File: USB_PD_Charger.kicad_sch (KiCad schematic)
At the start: 43 parts, among them J9 Conn_01x05, Q1 AON7403, U1 LM3489QMM/NOPB, U2 TPS65987DDHRSHR, U3 MX25L8006EM1I-12G

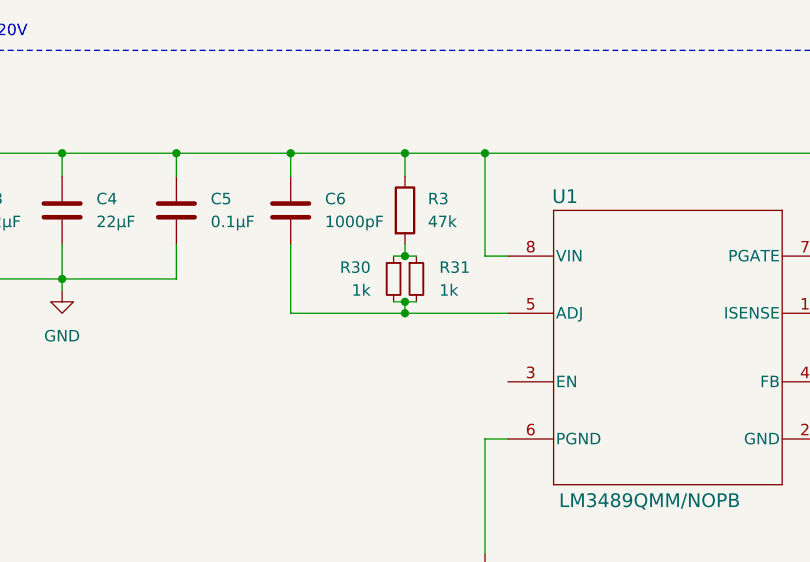
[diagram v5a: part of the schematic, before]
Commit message: Laid out components for power circuits
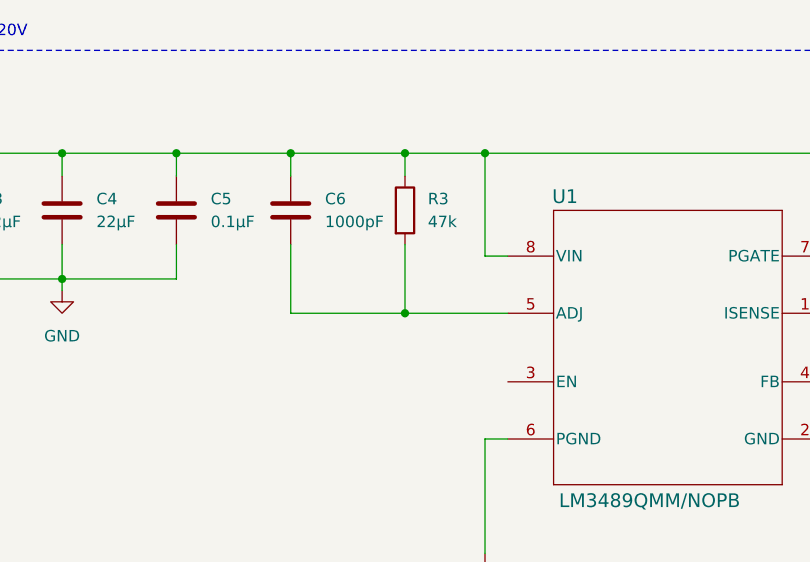
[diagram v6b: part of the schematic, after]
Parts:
- removed R30, R31: 1k, Resistor_SMD:R_0402_1005Metric, symbol Device:R_Small
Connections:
- net at R3.2: now also C6.2, U1.5 (ADJ)
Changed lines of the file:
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@@
 	)
 	(junction
-		(at 99.06 44.45)
-		(diameter 0)
-		(color 0 0 0 0)
-	)
-	(junction
 		(at 166.37 33.02)
 		(diameter 0)
@@
 	)
 	(junction
-		(at 99.06 50.8)
-		(diameter 0)
-		(color 0 0 0 0)
-	)
-	(junction
 		(at 231.14 113.03)
 		(diameter 0)
@@
 	)
 	(junction
-		(at 175.26 33.02)
+		(at 99.06 50.8)
 		(diameter 0)
 		(color 0 0 0 0)
 	)
 	(junction
-		(at 99.06 49.53)
+		(at 175.26 33.02)
 		(diameter 0)
 		(color 0 0 0 0)
@@
 	(wire
 		(pts
-			(xy 99.06 49.53) (xy 100.33 49.53)
-		)
-		(stroke
-			(width 0)
-			(type default)
-		)
-	)
-	(wire
-		(pts
 			(xy 109.22 125.73) (xy 111.76 125.73)
 		)
@@
 	(wire
 		(pts
-			(xy 99.06 43.18) (xy 99.06 44.45)
-		)
-		(stroke
-			(width 0)
-			(type default)
-		)
-	)
-	(wire
-		(pts
 			(xy 196.85 69.85) (xy 194.31 69.85)
 		)
@@
 	(wire
 		(pts
+			(xy 99.06 50.8) (xy 110.49 50.8)
+		)
+		(stroke
+			(width 0)
+			(type default)
+		)
+	)
+	(wire
+		(pts
 			(xy 252.73 31.75) (xy 252.73 33.02)
 		)
@@
 	(wire
 		(pts
-			(xy 86.36 50.8) (xy 99.06 50.8)
-		)
-		(stroke
-			(width 0)
-			(type default)
-		)
-	)
-	(wire
-		(pts
 			(xy 109.22 140.97) (xy 116.84 140.97)
 		)
@@
 	(wire
 		(pts
-			(xy 99.06 50.8) (xy 110.49 50.8)
+			(xy 86.36 50.8) (xy 99.06 50.8)
 		)
 		(stroke
@@
 	(wire
 		(pts
-			(xy 97.79 49.53) (xy 99.06 49.53)
-		)
-		(stroke
-			(width 0)
-			(type default)
-		)
-	)
-	(wire
-		(pts
 			(xy 142.24 121.92) (xy 142.24 120.65)
 		)
@@
 	(wire
 		(pts
-			(xy 99.06 44.45) (xy 100.33 44.45)
-		)
-		(stroke
-			(width 0)
-			(type default)
-		)
-	)
-	(wire
-		(pts
 			(xy 17.78 140.97) (xy 17.78 143.51)
 		)
@@
 	(wire
 		(pts
-			(xy 99.06 44.45) (xy 97.79 44.45)
+			(xy 99.06 43.18) (xy 99.06 50.8)
 		)
 		(stroke
@@
 	(wire
 		(pts
-			(xy 99.06 49.53) (xy 99.06 50.8)
-		)
-		(stroke
-			(width 0)
-			(type default)
-		)
-	)
-	(wire
-		(pts
 			(xy 146.05 44.45) (xy 156.21 44.45)
 		)
@@
 	)
 	(symbol
-		(lib_id "Device:R_Small")
-		(at 100.33 46.99 0)
-		(unit 1)
-		(exclude_from_sim no)
-		(in_bom yes)
-		(on_board yes)
-		(dnp no)
-		(property "Reference" "R31"
-			(at 102.87 45.7199 0)
-			(effects
-				(font
-					(size 1.27 1.27)
-				)
-				(justify left)
-			)
-		)
-		(property "Value" "1k"
-			(at 102.87 48.2599 0)
-			(effects
-				(font
-					(size 1.27 1.27)
-				)
-				(justify left)
-			)
-		)
-		(property "Footprint" "Resistor_SMD:R_0402_1005Metric"
-			(at 100.33 46.99 0)
-			(effects
-				(font
-					(size 1.27 1.27)
-				)
-				(hide yes)
-			)
-		)
-		(property "Datasheet" "~"
-			(at 100.33 46.99 0)
-			(effects
-				(font
-					(size 1.27 1.27)
-				)
-				(hide yes)
-			)
-		)
-		(property "Description" "Resistor, small symbol"
-			(at 100.33 46.99 0)
-			(effects
-				(font
-					(size 1.27 1.27)
-				)
-				(hide yes)
-			)
-		)
-		(property "Part_Number" "0402WGF1001TCE"
-			(at 100.33 46.99 0)
-			(effects
-				(font
-					(size 1.27 1.27)
-				)
-				(hide yes)
-			)
-		)
-		(property "LCSC" "C11702"
-			(at 100.33 46.99 0)
-			(effects
-				(font
-					(size 1.27 1.27)
-				)
-				(hide yes)
-			)
-		)
-		(pin "1"
-		)
-		(pin "2"
-		)
-		(instances
-			(project "XG_Mobile_Dock"
-				(path "/f97e6956-ab08-42cb-8fed-03fa58e87f0e/fa35204a-fbf7-48de-bc5b-11fc2e29f675"
-					(reference "R31")
-					(unit 1)
-				)
-			)
-		)
-	)
-	(symbol
 		(lib_id "Device:R")
 		(at 196.85 118.11 0)
@@
 					(unit 1)
 				)
-			)
-		)
-	)
-	(symbol
-		(lib_id "Device:R_Small")
-		(at 97.79 46.99 0)
-		(mirror y)
-		(unit 1)
-		(exclude_from_sim no)
-		(in_bom yes)
-		(on_board yes)
-		(dnp no)
-		(property "Reference" "R30"
-			(at 95.25 45.7199 0)
-			(effects
-				(font
-					(size 1.27 1.27)
-				)
-				(justify left)
-			)
-		)
-		(property "Value" "1k"
-			(at 95.25 48.2599 0)
-			(effects
-				(font
-					(size 1.27 1.27)
-				)
-				(justify left)
-			)
-		)
-		(property "Footprint" "Resistor_SMD:R_0402_1005Metric"
-			(at 97.79 46.99 0)
-			(effects
-				(font
-					(size 1.27 1.27)
-				)
-				(hide yes)
-			)
-		)
-		(property "Datasheet" "~"
-			(at 97.79 46.99 0)
-			(effects
-				(font
-					(size 1.27 1.27)
-				)
-				(hide yes)
-			)
-		)
-		(property "Description" "Resistor, small symbol"
-			(at 97.79 46.99 0)
-			(effects
-				(font
-					(size 1.27 1.27)
-				)
-				(hide yes)
-			)
-		)
-		(property "Part_Number" "0402WGF1001TCE"
-			(at 97.79 46.99 0)
-			(effects
-				(font
-					(size 1.27 1.27)
-				)
-				(hide yes)
-			)
-		)
-		(property "LCSC" "C11702"
-			(at 97.79 46.99 0)
-			(effects
-				(font
-					(size 1.27 1.27)
-				)
-				(hide yes)
-			)
-		)
-		(pin "1"
-		)
-		(pin "2"
-		)
-		(instances
-			(project "XG_Mobile_Dock"
-				(path "/f97e6956-ab08-42cb-8fed-03fa58e87f0e/fa35204a-fbf7-48de-bc5b-11fc2e29f675"
-					(reference "R30")
-					(unit 1)
-				)

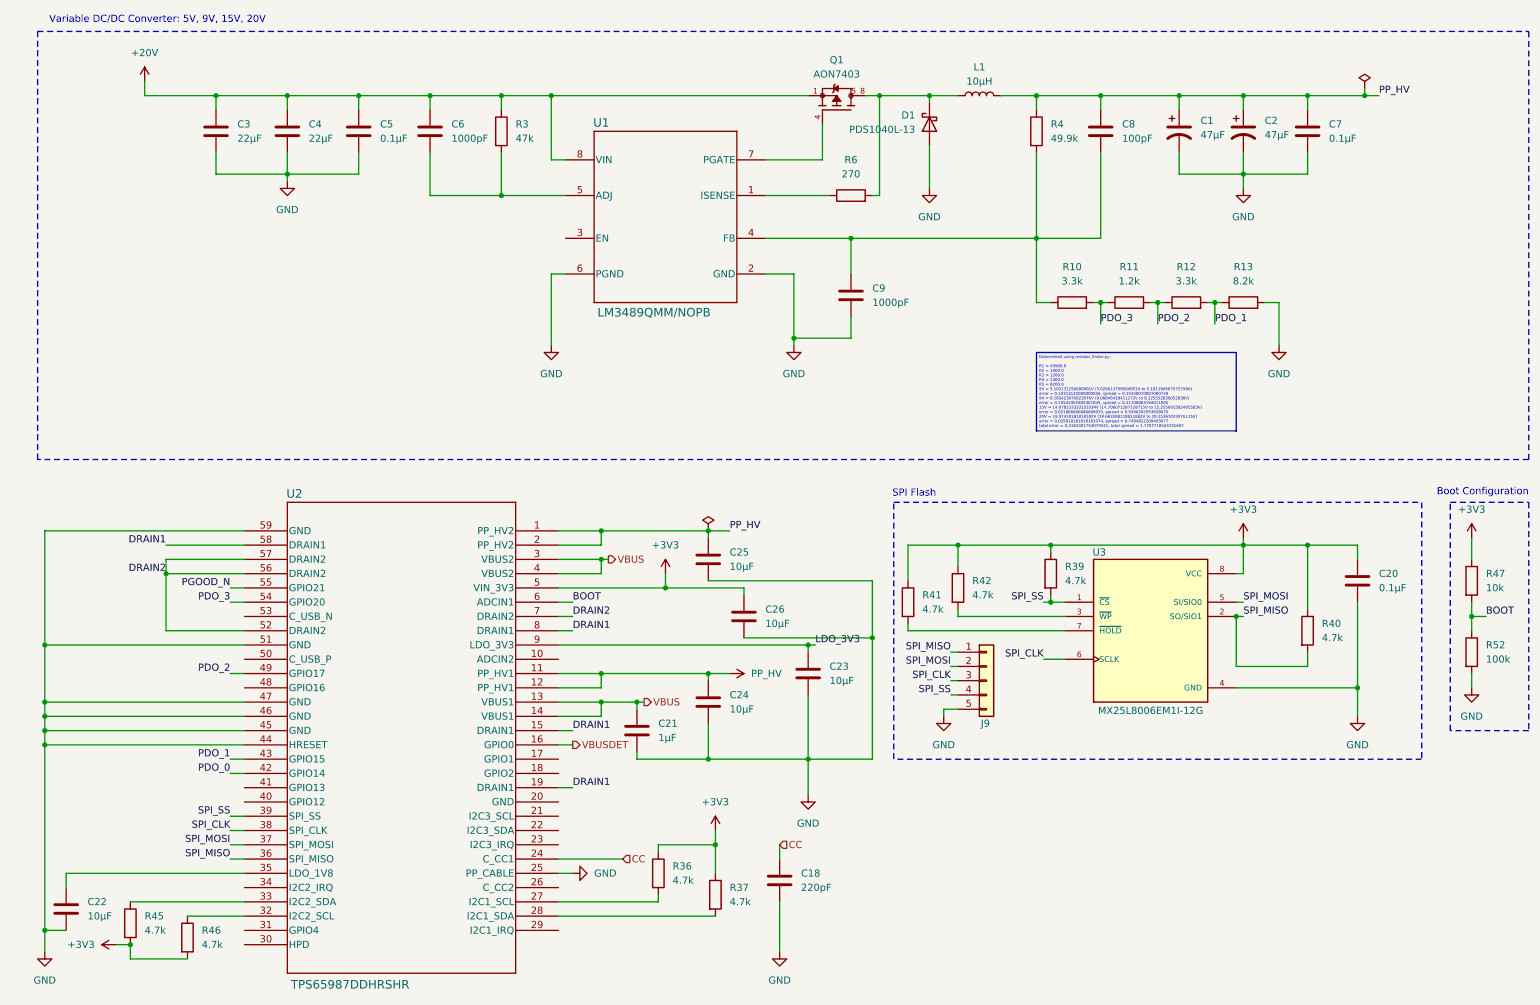
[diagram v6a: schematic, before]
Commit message: Added MCU
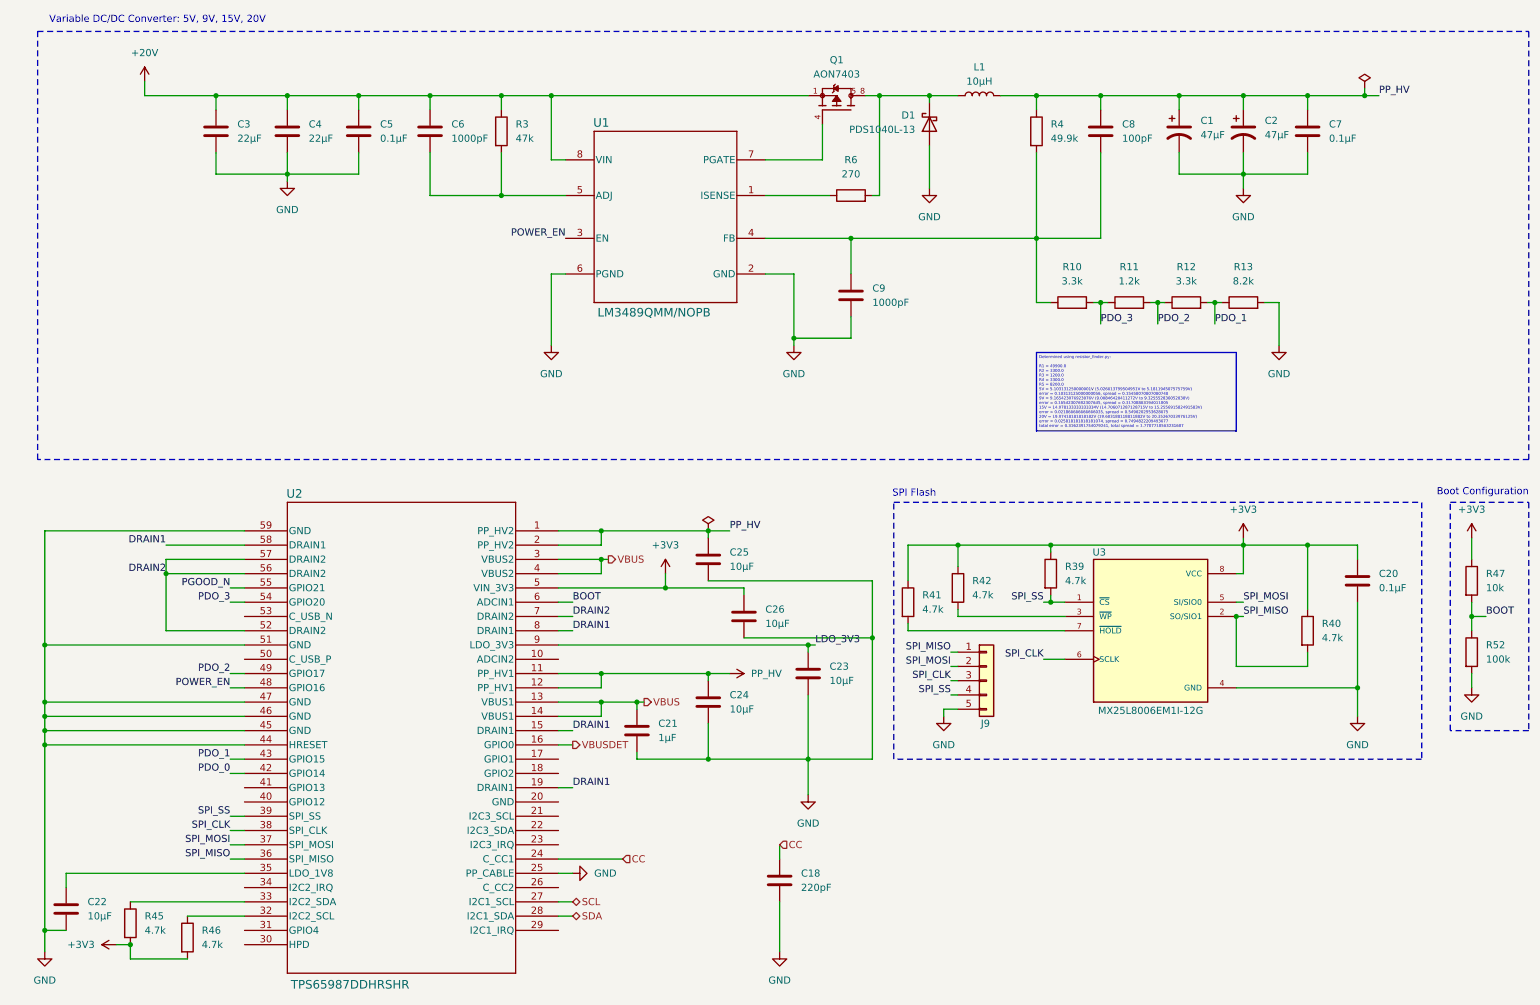
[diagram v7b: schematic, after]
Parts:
- removed R36, R37: 4.7k, Resistor_SMD:R_0402_1005Metric, symbol Device:R
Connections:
- net SDA: now reaches U2.28 (I2C1_SDA)
- net POWER_EN: now reaches U1.3 (EN)
- net POWER_EN: now also U2.48 (GPIO16)
- net SCL: now reaches U2.27 (I2C1_SCL)

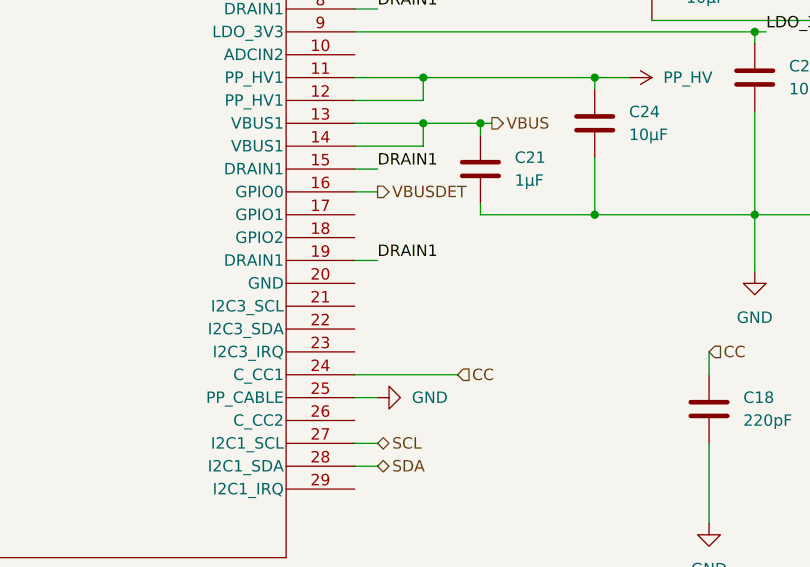
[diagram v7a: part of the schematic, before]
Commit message: Fixed all DRC errors
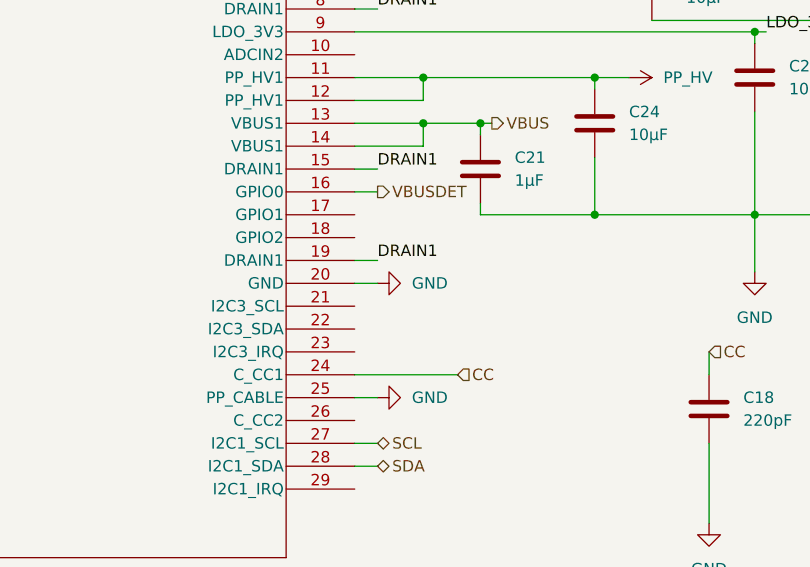
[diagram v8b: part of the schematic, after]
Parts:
- U1: footprint LM3489QMM-NOPB -> LM3489QMM-NOPB:LM3489QMM-NOPB
- U2: footprint TPS65987DDHRSHR -> TPS65987DDHRSHR:TPS65987DDHRSHR
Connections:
- net GND: now also U2.20 (GND)
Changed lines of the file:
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@@
 	(wire
 		(pts
+			(xy 109.22 158.75) (xy 111.76 158.75)
+		)
+		(stroke
+			(width 0)
+			(type default)
+		)
+	)
+	(wire
+		(pts
 			(xy 53.34 123.19) (xy 50.8 123.19)
 		)
@@
 	)
 	(symbol
+		(lib_id "power:GND")
+		(at 111.76 158.75 90)
+		(unit 1)
+		(exclude_from_sim no)
+		(in_bom yes)
+		(on_board yes)
+		(dnp no)
+		(fields_autoplaced yes)
+		(property "Reference" "#PWR080"
+			(at 118.11 158.75 0)
+			(effects
+				(font
+					(size 1.27 1.27)
+				)
+				(hide yes)
+			)
+		)
+		(property "Value" "GND"
+			(at 115.57 158.7499 90)
+			(effects
+				(font
+					(size 1.27 1.27)
+				)
+				(justify right)
+			)
+		)
+		(property "Footprint" ""
+			(at 111.76 158.75 0)
+			(effects
+				(font
+					(size 1.27 1.27)
+				)
+				(hide yes)
+			)
+		)
+		(property "Datasheet" ""
+			(at 111.76 158.75 0)
+			(effects
+				(font
+					(size 1.27 1.27)
+				)
+				(hide yes)
+			)
+		)
+		(property "Description" "Power symbol creates a global label with name \"GND\" , ground"
+			(at 111.76 158.75 0)
+			(effects
+				(font
+					(size 1.27 1.27)
+				)
+				(hide yes)
+			)
+		)
+		(pin "1"
+		)
+		(instances
+			(project "XG_Mobile_Dock"
+				(path "/f97e6956-ab08-42cb-8fed-03fa58e87f0e/fa35204a-fbf7-48de-bc5b-11fc2e29f675"
+					(reference "#PWR080")
+					(unit 1)
+				)
+			)
+		)
+	)
+	(symbol
 		(lib_id "Device:R")
 		(at 220.98 69.85 90)
@@
 			)
 		)
-		(property "Footprint" "LM3489QMM-NOPB"
+		(property "Footprint" "LM3489QMM-NOPB:LM3489QMM-NOPB"
 			(at 128.27 54.61 0)
 			(effects
@@
 			)
 		)
-		(property "Footprint" "TPS65987DDHRSHR"
+		(property "Footprint" "TPS65987DDHRSHR:TPS65987DDHRSHR"
 			(at 109.22 110.49 0)
 			(effects
